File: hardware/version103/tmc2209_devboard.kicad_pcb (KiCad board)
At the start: 2 copper layers, 69 x 53.8 mm, 41 parts, among them J1 Conn_01x02_Male, J2 Conn_01x03_Pin, J4 motor_conn, J5 motor_conn, J6 motor_conn, SW1 SW_Push, U1 TMC2209-LA

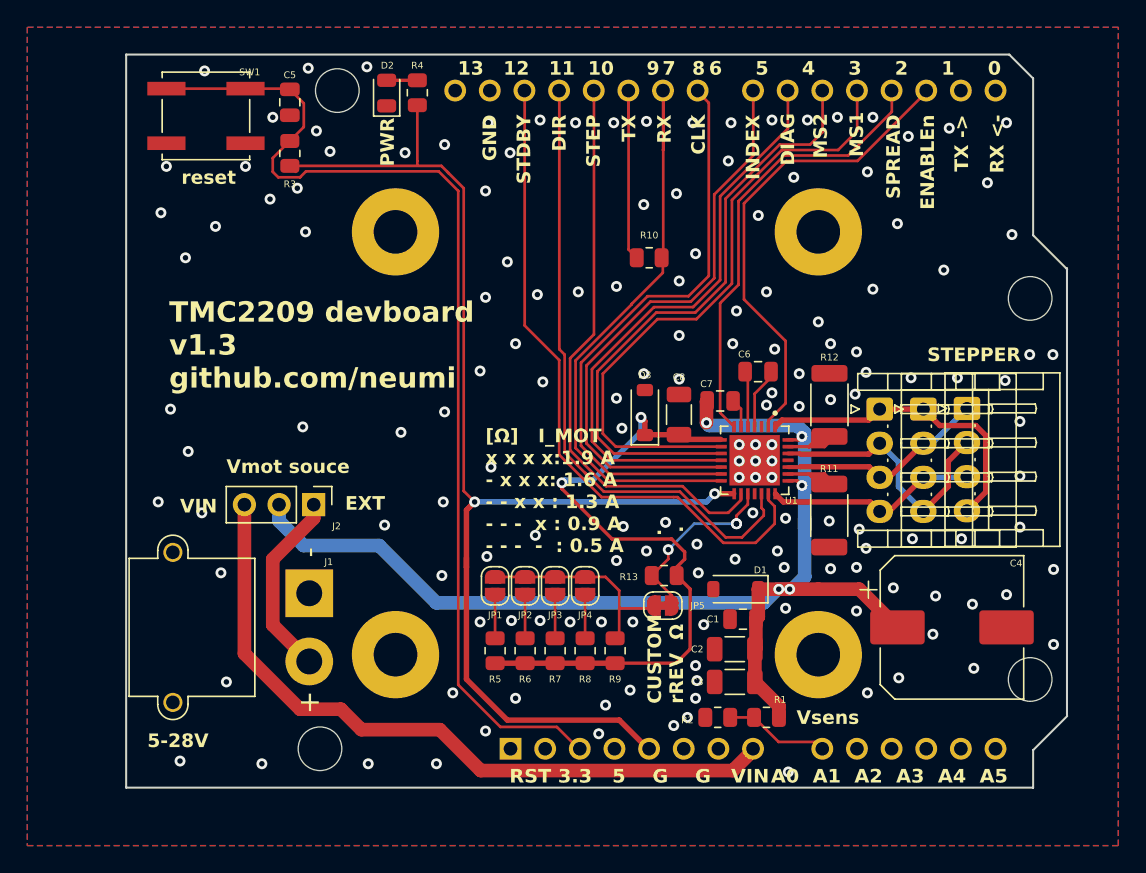
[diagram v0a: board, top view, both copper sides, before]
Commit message: changed motor power source connector and elec cap for lower nema17 placement. Added production files for 103
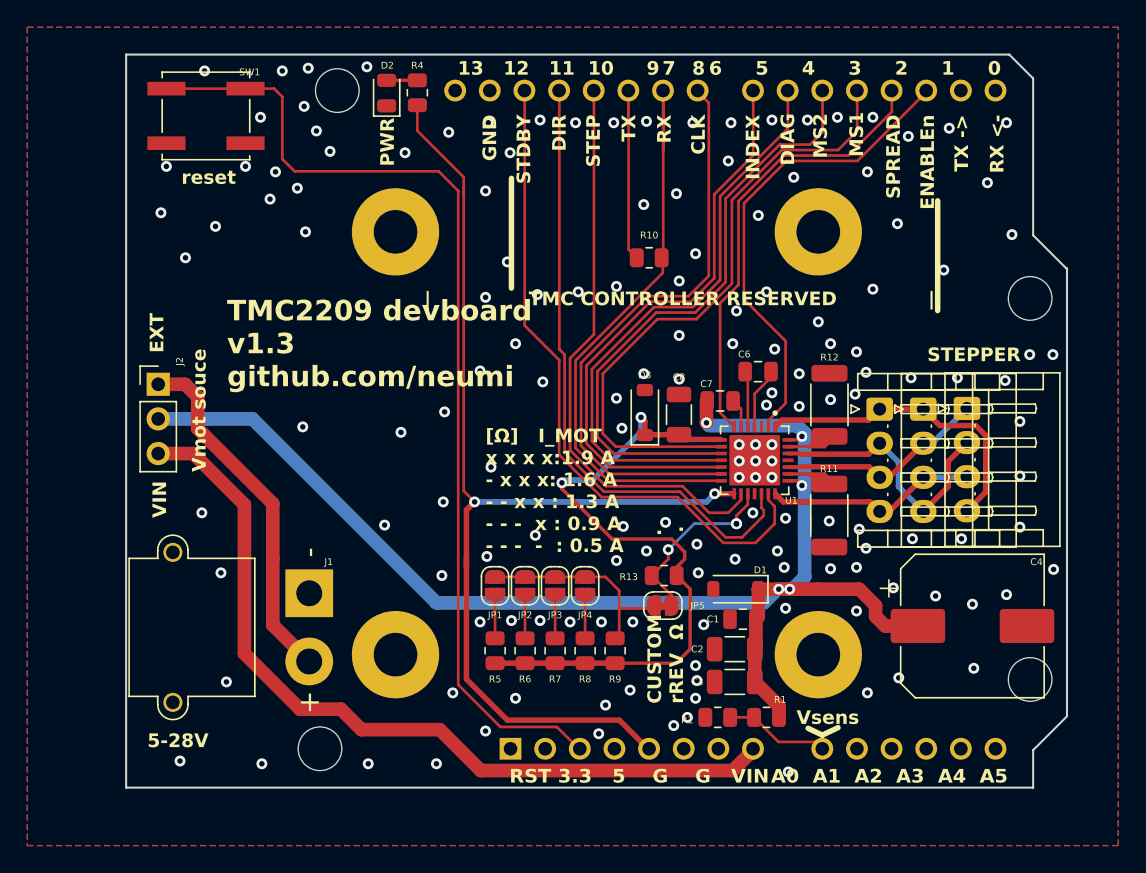
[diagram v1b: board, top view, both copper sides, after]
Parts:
- removed C5: C100nF, Capacitor_SMD:C_0805_2012Metric
- removed R3: R10k, Resistor_SMD:R_0805_2012Metric
- moved J2 14.4 mm to (44.6, 46.2), turned to 0 degrees
- moved C4 1.50 mm to (104.3, 63.9)
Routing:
- net Vdrive: track 87.4 -> 100.0 mm
- net +28V: track 13.9 -> 26.1 mm
- net +5V: track 91.2 -> 80.8 mm
- net Net-(A1-VIN): track 52.4 -> 60.3 mm
- net rst: track 78.2 -> 74.3 mm
- net GND: vias 148 -> 146
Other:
- board text added: "| TMC CONTROLLER RESERVED |"

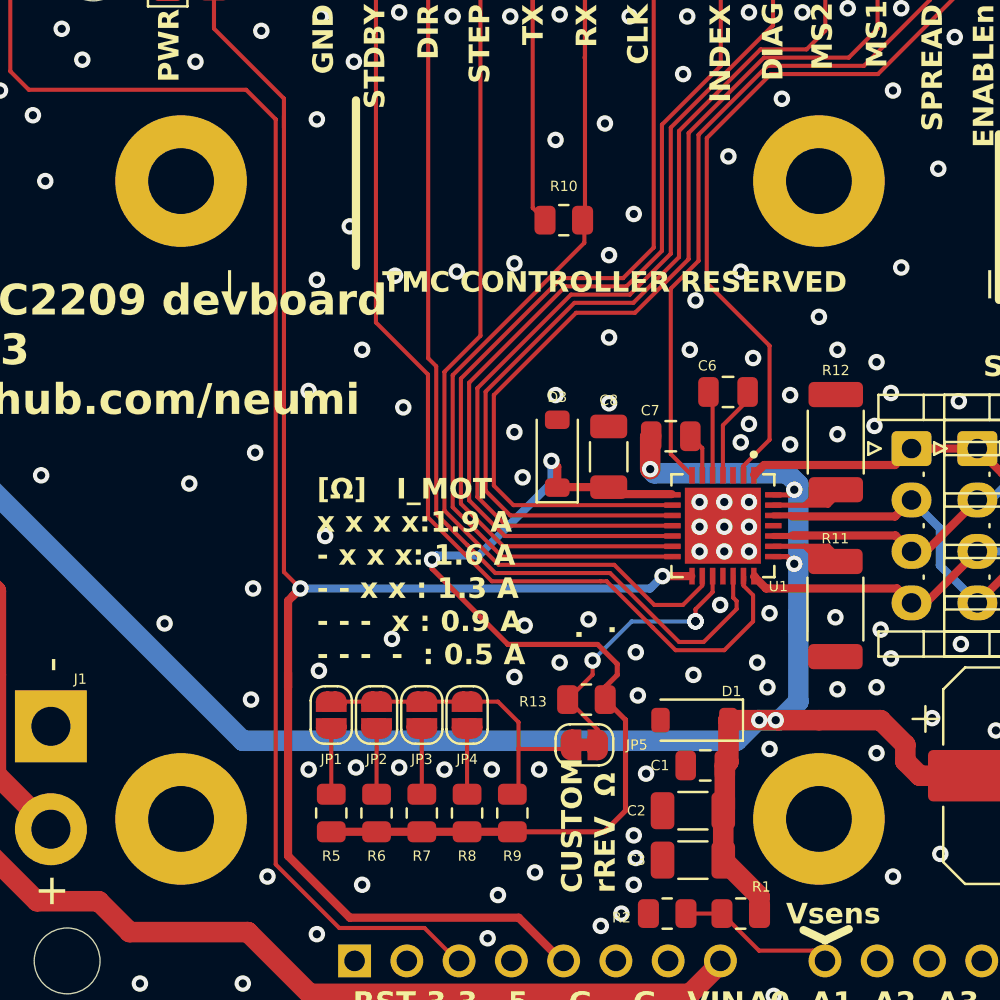
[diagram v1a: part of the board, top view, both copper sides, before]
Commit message: added gnd connection to motor mounts, added DNP for static PCB footprints
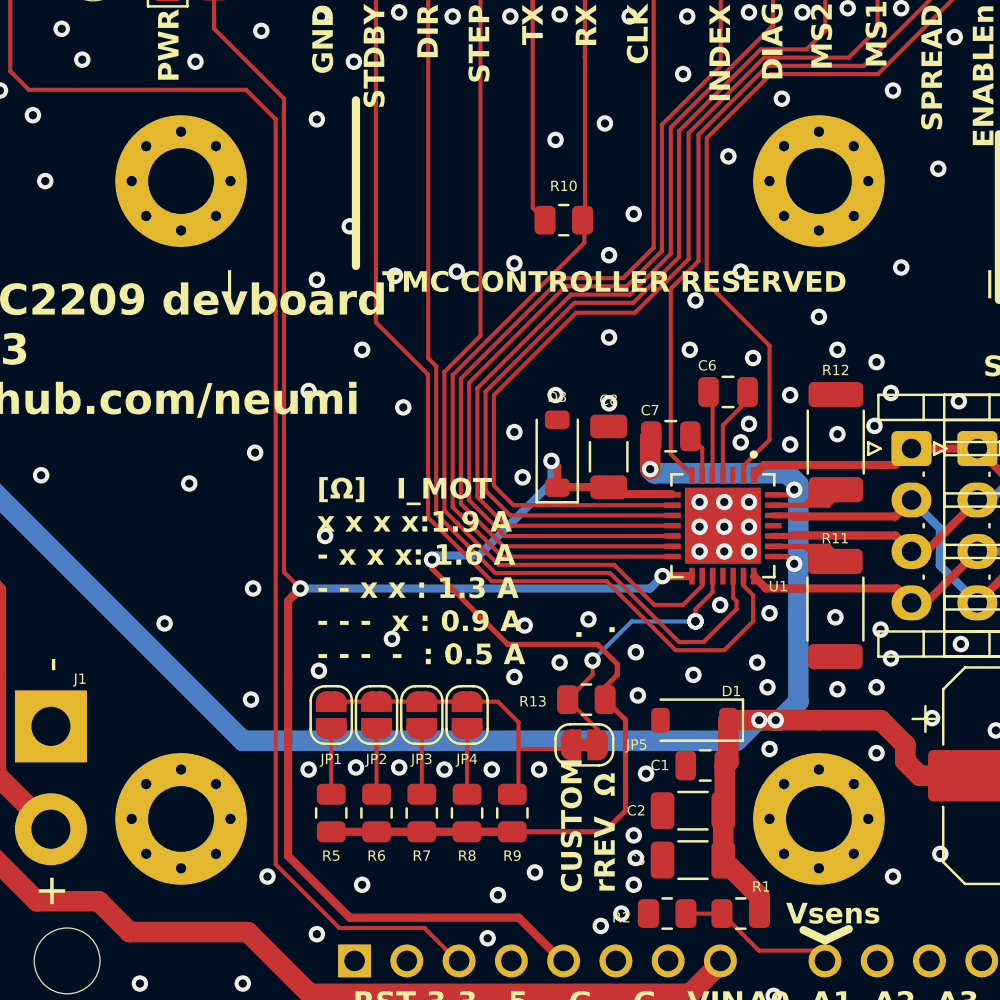
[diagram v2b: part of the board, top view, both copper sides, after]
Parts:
- H1, H2, H3, H4: value MountingHole -> MountingHole_Pad; footprint MountingHole:MountingHole_3.2mm_M3_Pad -> MountingHole:MountingHole_3.2mm_M3_Pad_Via
- moved H1 31.0 mm to (93.0, 35.0)
- moved H2 31.0 mm to (93.0, 66.0)
- moved H3 31.0 mm to (62.0, 66.0)
- moved H4 31.0 mm to (62.0, 35.0)
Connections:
- H1 pad 1: (no net) -> GND
- H2 pad 1: (no net) -> GND
- H3 pad 1: (no net) -> GND
- H4 pad 1: (no net) -> GND

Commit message: minor design changes, added produciton files for version 103
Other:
- outline, holes or cut-outs redrawn
